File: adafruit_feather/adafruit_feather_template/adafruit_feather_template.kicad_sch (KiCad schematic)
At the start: 16 parts, among them J1 4040_Header_Male_Vert_12pin_0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, J2 4039_Header_Male_Vert_16pin_0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, J3 3096_USBC_RA_SMD, Q1 4043_DMG3414_Nch_Mosfet_SOT23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, SW1 RST, U1 4042_MCP73831_Battery_Charger, U2 CRG, U3 PWR, U4 3093_MIC5225_3v3

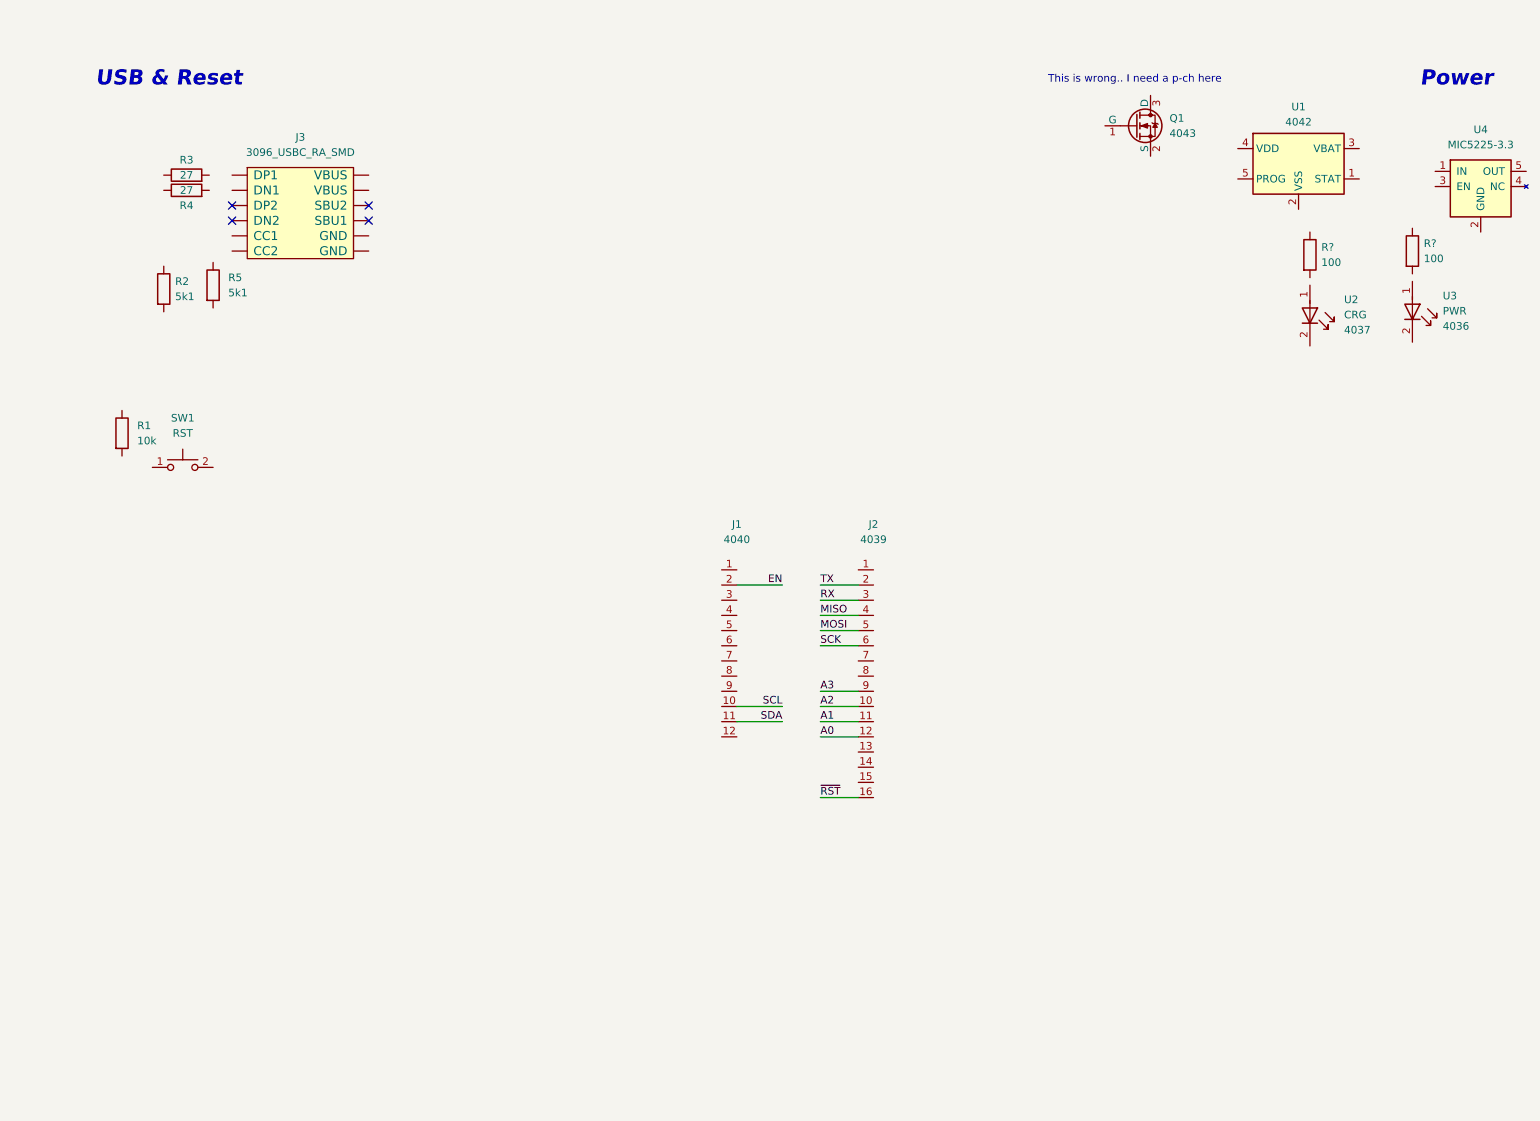
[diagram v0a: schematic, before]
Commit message: Added some more of the LiPo circuitry, LEDs, and connectors
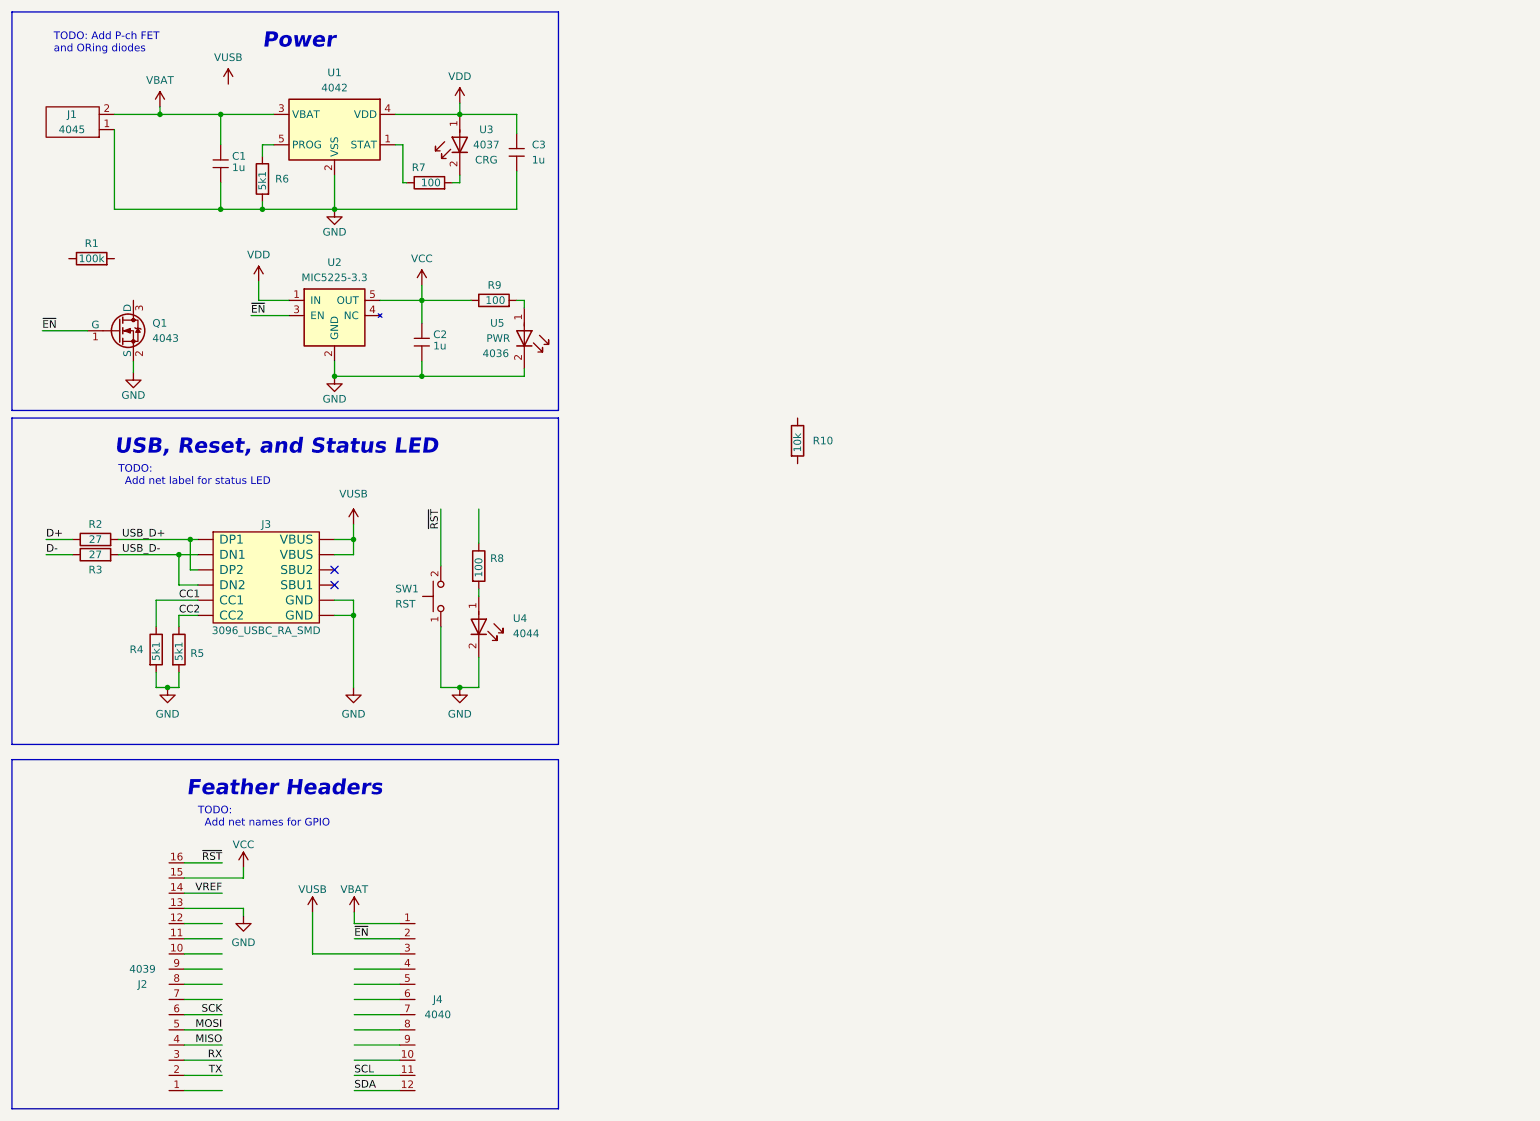
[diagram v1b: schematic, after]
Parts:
- added C1, C2, C3: 4013_Capacitor_1u_16V_0402, Shulltronics_Generics:C_0402_HandSolder, symbol Shulltronics_Passives:4013_Capacitor_1u_16V_0402
- added J1: 4045_Connector_PH_2pos_RA_SMD, Shulltronics_Connectors:4045_JST_PH_2pos_RA_SMD, symbol Shulltronics_Connectors:4045_Connector_PH_2pos_RA_SMD
- added R1: 4017_Resistor_SMD_100k_0.125W_1%_1, Shulltronics_Generics:RES-0402, symbol Shulltronics_Passives:4017_Resistor_SMD_100k_0.125W_1%_1
- added R6: 4009_Resistor_SMD_5k1_0.10W_1%, Shulltronics_Generics:RES-0402, symbol Shulltronics_Passives:4009_Resistor_SMD_5k1_0.10W_1%
- added R8: 4038_Resistor_SMD_100_0.125W_1%, Shulltronics_Generics:RES-0402, symbol Shulltronics_Passives:4038_Resistor_SMD_100_0.125W_1%
- added U4: 4044_LED_RED_SMD, Shulltronics_Generics:LED_0402, symbol Shulltronics_Opto:4044_LED_RED_SMD
- gave numbers to parts that had none: 2
- renumbered J1 to J4, R1 to R10, R3 to R2, R4 to R3, R2 to R4, U4 to U2, U2 to U3, U3 to U5
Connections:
- net EN is gone; now on net ~{EN}: J4.2
- net SCL: now also J4.11; no longer J4.10
- net SDA: now also J4.12; no longer J4.11
- net ~{RST}: now also SW1.2
- net VDD: now reaches U2.1 (IN)
- net VDD: now also U1.4 (VDD), U3.1 (A), C3.2
- net GND: now reaches U2.2 (GND)
- net GND: now also J2.13, J3.A1/B12 (GND), J3.B1/A12 (GND), Q1.2 (S), R4.2, R5.2, SW1.1, U1.2 (VSS), U5.2 (K), C1.1, C2.1, C3.1, J1.1, R6.2, U4.2 (K)
- net ~{EN}: now reaches U2.3 (EN)
- net ~{EN}: now also Q1.1 (G)
- net VCC: now reaches U2.5 (OUT)
- net VCC: now also J2.15, R9.1, C2.2
- net at R9.2: now also U5.1 (A)
- net at U1.1 (STAT): now also R7.1
- net VBAT: now reaches U1.3 (VBAT)
- net VBAT: now also J4.1, C1.2, J1.2
- net at U1.5 (PROG): now also R6.1
- net D+: now reaches R2.1
- net USB_D+: now reaches R2.2
- net USB_D+: now also J3.A6 (DP1), J3.B6 (DP2)
- net VUSB: now reaches J3.A4/B9 (VBUS)
- net VUSB: now also J3.B4/A9 (VBUS), J4.3
- net CC1: now reaches J3.A5 (CC1)
- net CC1: now also R4.1
- net USB_D-: now reaches J3.A7 (DN1)
- net USB_D-: now also J3.B7 (DN2), R3.2
- net CC2: now reaches J3.B5 (CC2)
- net CC2: now also R5.1
- net VREF: now reaches J2.14
- net at U3.2 (K): now also R7.2
- net D-: now reaches R3.1
- net A0: no longer names the net of J2.12
- net A1: no longer names the net of J2.11
- net A2: no longer names the net of J2.10
- net A3: no longer names the net of J2.9
- new net: R8.2, U4.1 (A)
- no-connect marks 4 -> 2
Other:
- note added: "Feather Headers"
- note added: "TODO: Add P-ch FET and ORing diodes"
- note added: "TODO: Add net label for status LED"
- note added: "TODO: Add net names for GPIO"
- note added: "USB, Reset, and Status LED"
- note removed: "This is wrong.. I need a p-ch here"
- note removed: "USB & Reset"
- moved on the sheet: J2, J3, J4, Q1, R10, R2, R3, R4, R5, R7, R9, SW1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
